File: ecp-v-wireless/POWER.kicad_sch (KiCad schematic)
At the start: 1 part, among them U2 LFE5U-85F-6BG381x

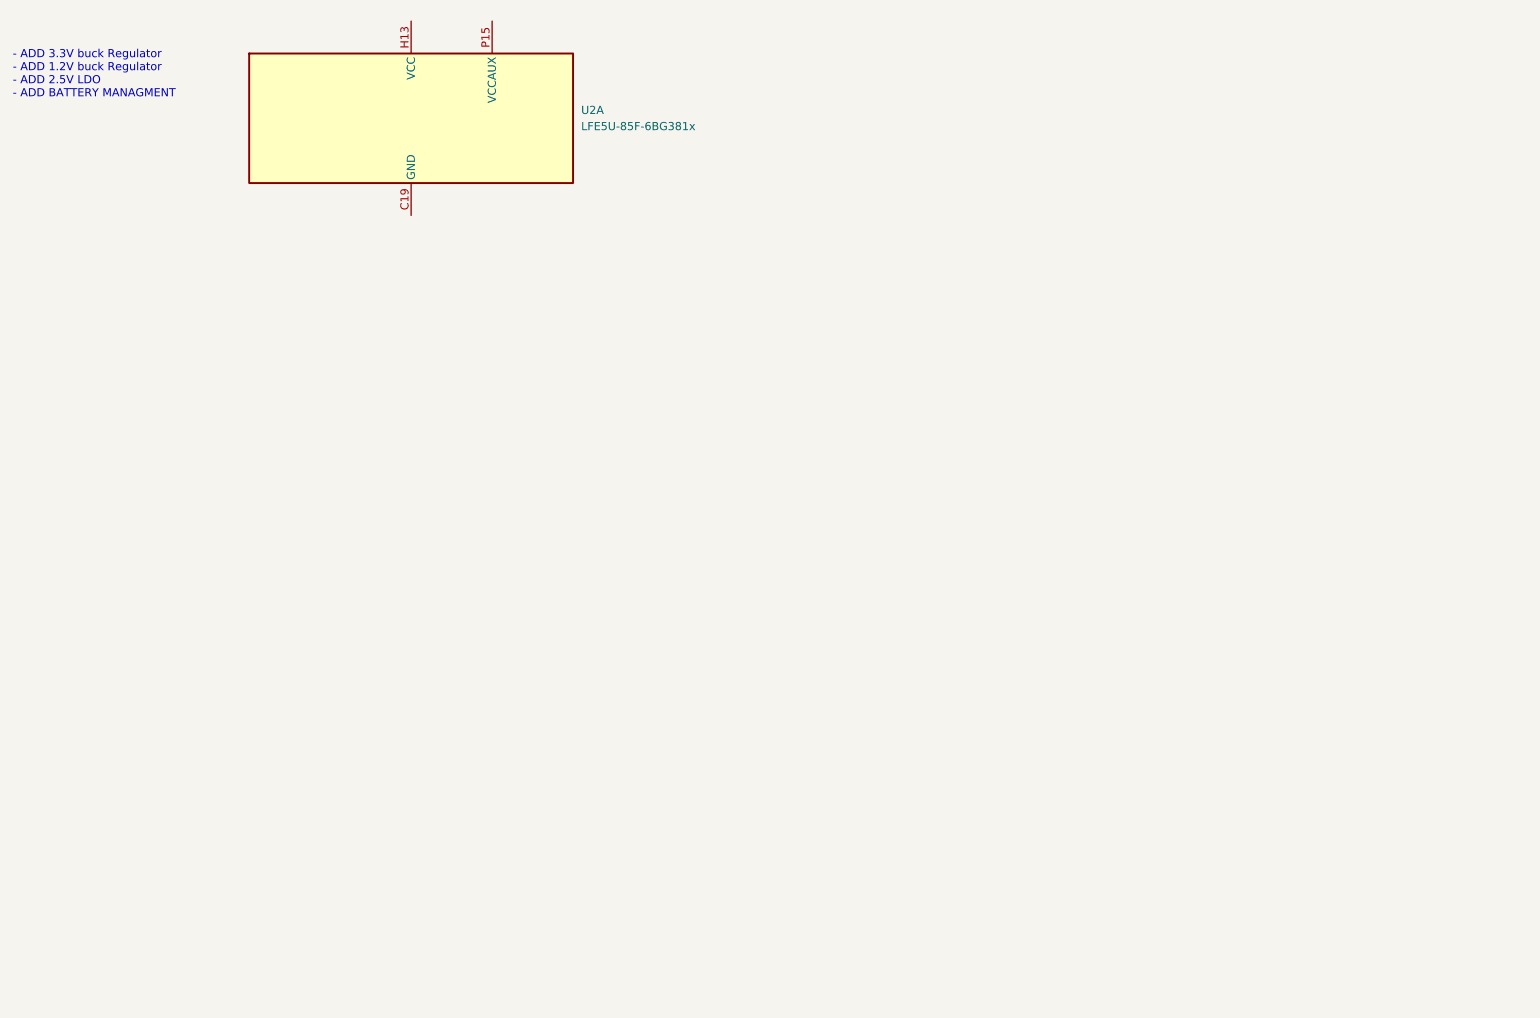
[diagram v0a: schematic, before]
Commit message: Add block diagram, USB, LiPo MGMT, Regs, etc
Signed-off-by: Michael Welling <mwelling79@gmail.com>
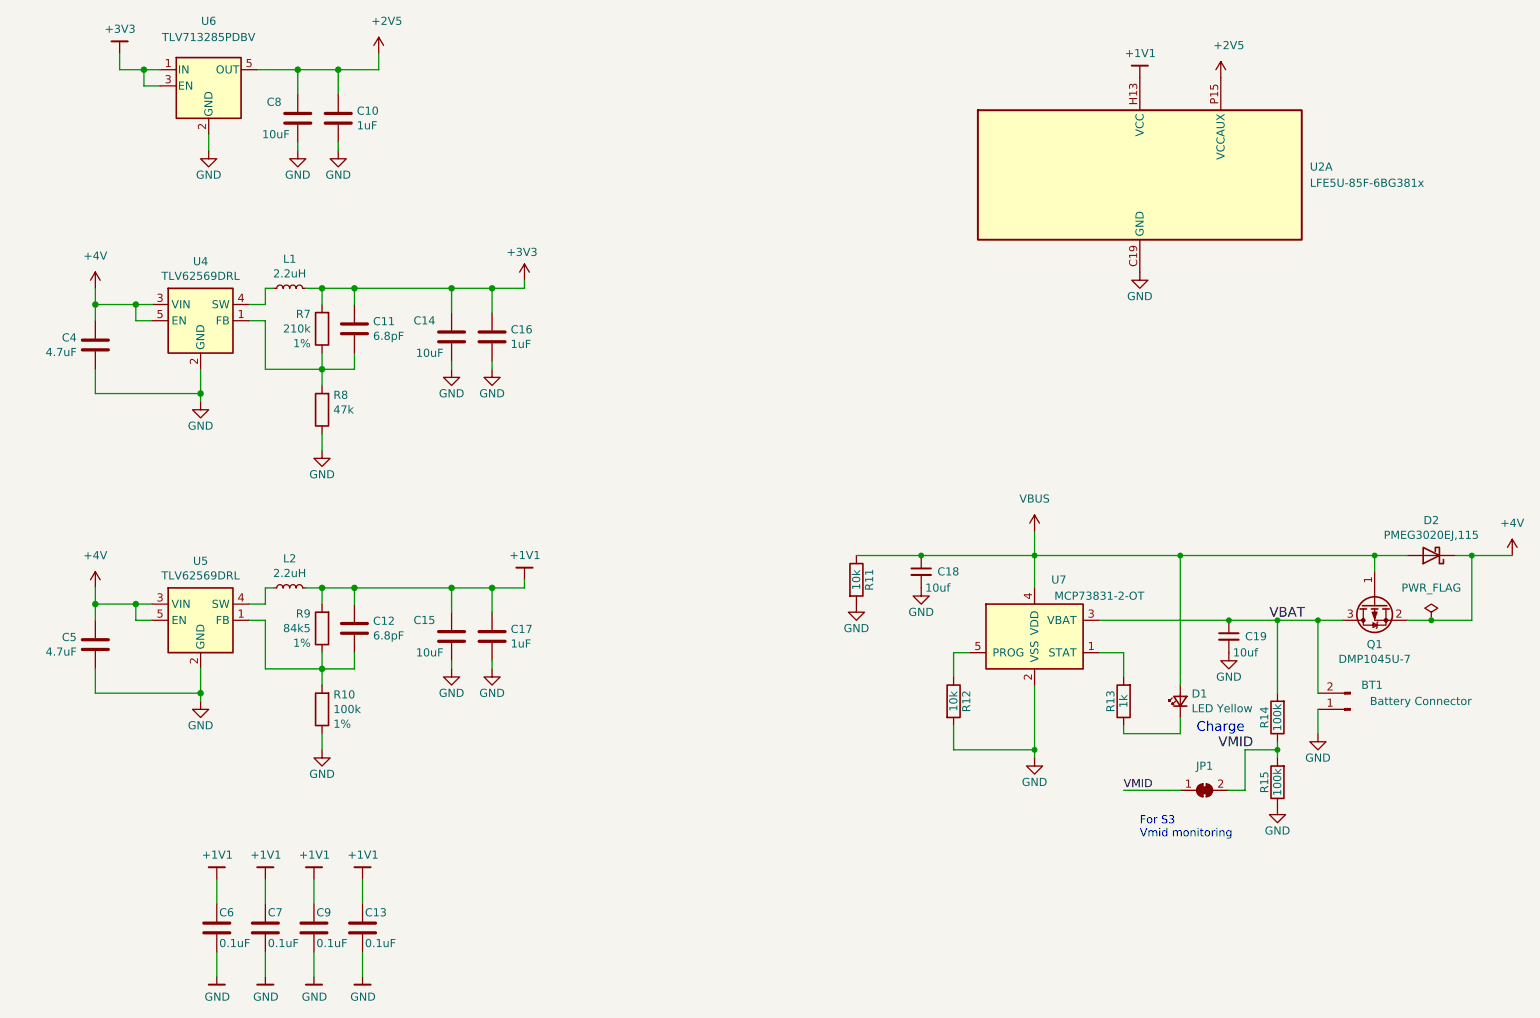
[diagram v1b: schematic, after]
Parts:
- added BT1: Battery Connector, Connector_JST:JST_PH_B2B-PH-SM4-TB_1x02-1MP_P2.00mm_Vertical, symbol Connector:Conn_01x02_Male
- added C10, C16, C17: 1uF, Capacitor_SMD:C_0402_1005Metric, symbol Device:C
- added C11, C12: 6.8pF, Capacitor_SMD:C_0402_1005Metric, symbol Device:C
- added C13, C6, C7, C9: 0.1uF, Capacitor_SMD:C_0402_1005Metric, symbol Device:C
- added C14, C15, C8: 10uF, Capacitor_SMD:C_0603_1608Metric, symbol Device:C
- added C18, C19: 10uf, Capacitor_SMD:C_0805_2012Metric, symbol Device:C_Small
- added C4, C5: 4.7uF, Capacitor_SMD:C_0402_1005Metric, symbol Device:C
- added D1: LED Yellow, LED_SMD:LED_0603_1608Metric, symbol Device:LED_Small
- added D2: PMEG3020EJ,115, Diode_SMD:D_SOD-323F, symbol Device:D_Schottky
- added JP1: SolderJumper_2_Bridged, Jumper:SolderJumper-2_P1.3mm_Bridged_RoundedPad1.0x1.5mm, symbol Jumper:SolderJumper_2_Bridged
- added L1, L2: 2.2uH, Inductor_SMD:L_0805_2012Metric, symbol Device:L_Small
- added Q1: DMP1045U-7, Package_TO_SOT_SMD:SOT-23, symbol Device:Q_PMOS_GSD
- added R10: 100k, Resistor_SMD:R_0402_1005Metric, symbol Device:R
- added R11, R12: 10k, Resistor_SMD:R_0603_1608Metric, symbol Device:R
- added R13: 1k, Resistor_SMD:R_0603_1608Metric, symbol Device:R
- added R14, R15: 100k, Resistor_SMD:R_0603_1608Metric, symbol Device:R
- added R7: 210k, Resistor_SMD:R_0402_1005Metric, symbol Device:R
- added R8: 47k, Resistor_SMD:R_0402_1005Metric, symbol Device:R
- added R9: 84k5, Resistor_SMD:R_0402_1005Metric, symbol Device:R
- added U4, U5: TLV62569DRL, Package_TO_SOT_SMD:SOT-666, symbol Regulator_Switching:TLV62569DRL
- added U6: TLV713285PDBV, Package_TO_SOT_SMD:SOT-23-5, symbol Regulator_Linear:TLV713285PDBV
- added U7: MCP73831-2-OT, Package_TO_SOT_SMD:SOT-23-5, symbol Battery_Management:MCP73831-2-OT
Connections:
- net GND: now reaches U2.B14 (GND), U2.B7 (GND), U2.C19 (GND), U2.D4 (GND), U2.F13 (GND), U2.F14 (GND), U2.F7 (GND), U2.F8 (GND), U2.G10 (GND), U2.G11 (GND), U2.G12 (GND), U2.G13 (GND), U2.G14 (GND), U2.G15 (GND), U2.G17 (GND), U2.G4 (GND), U2.G6 (GND), U2.G7 (GND), U2.G8 (GND), U2.G9 (GND), U2.H19 (GND), U2.J10 (GND), U2.J11 (GND), U2.J12 (GND), U2.J14 (GND), U2.J2 (GND), U2.J7 (GND), U2.J9 (GND), U2.K10 (GND), U2.K11 (GND), U2.K12 (GND), U2.K14 (GND), U2.K15 (GND), U2.K6 (GND), U2.K7 (GND), U2.K9 (GND), U2.L10 (GND), U2.L11 (GND), U2.L12 (GND), U2.L9 (GND), U2.M10 (GND), U2.M11 (GND), U2.M12 (GND), U2.M14 (GND), U2.M16 (GND), U2.M2 (GND), U2.M7 (GND), U2.M9 (GND), U2.N14 (GND), U2.N15 (GND), U2.N6 (GND), U2.N7 (GND), U2.P11 (GND), U2.P12 (GND), U2.P13 (GND), U2.P14 (GND), U2.P7 (GND), U2.P8 (GND), U2.R19 (GND), U2.T10 (GND), U2.T11 (GND), U2.T12 (GND), U2.T13 (GND), U2.T14 (GND), U2.T15 (GND), U2.T6 (GND), U2.T7 (GND), U2.T8 (GND), U2.T9 (GND), U2.U10 (GND), U2.U11 (GND), U2.U12 (GND), U2.U13 (GND), U2.U14 (GND), U2.U15 (GND), U2.U6 (GND), U2.U7 (GND), U2.U8 (GND), U2.U9 (GND), U2.V10 (GND), U2.V11 (GND), U2.V12 (GND), U2.V13 (GND), U2.V14 (GND), U2.V15 (GND), U2.V16 (GND), U2.V17 (GND), U2.V18 (GND), U2.V19 (GND), U2.V20 (GND), U2.V5 (GND), U2.V6 (GND), U2.V7 (GND), U2.V8 (GND), U2.V9 (GND), U2.W12 (GND), U2.W15 (GND), U2.W16 (GND), U2.W19 (GND), U2.W20 (GND), U2.W6 (GND), U2.W7 (GND), U2.Y11 (GND), U2.Y12 (GND), U2.Y14 (GND), U2.Y15 (GND), U2.Y16 (GND), U2.Y17 (GND), U2.Y19 (GND), U2.Y5 (GND), U2.Y6 (GND), U2.Y7 (GND), U2.Y8 (GND)
- net GND: now also BT1.1 (Pin_1), C10.2, C13.2, C14.2, C15.2, C16.2, C17.2, C18.2, C19.2, C4.2, C5.2, C6.2, C7.2, C8.2, C9.2, R10.1, R11.2, R12.2, R15.1, R8.1, U4.2 (GND), U5.2 (GND), U6.2 (GND), U7.2 (VSS)
- net +2V5: now reaches U2.F15 (VCCAUX), U2.F6 (VCCAUX), U2.P15 (VCCAUX), U2.P6 (VCCAUX)
- net +2V5: now also C10.1, C8.1, U6.5 (OUT)
- net +1V1: now reaches U2.H10 (VCC), U2.H11 (VCC), U2.H12 (VCC), U2.H13 (VCC), U2.H8 (VCC), U2.H9 (VCC), U2.J13 (VCC), U2.J8 (VCC), U2.K13 (VCC), U2.K8 (VCC), U2.L13 (VCC), U2.L8 (VCC), U2.M13 (VCC), U2.M8 (VCC), U2.N10 (VCC), U2.N11 (VCC), U2.N12 (VCC), U2.N13 (VCC), U2.N8 (VCC), U2.N9 (VCC)
- net +1V1: now also C12.1, C13.1, C15.1, C17.1, C6.1, C7.1, C9.1, L2.2, R9.2
- new net: R13.2, U7.1 (STAT)
- new net: R12.1, U7.5 (PROG)
- new net: L2.1, U5.4 (SW)
- new net: C11.2, R7.1, R8.2, U4.1 (FB)
- new net: C12.2, R10.2, R9.1, U5.1 (FB)
- new net: D1.1 (K), R13.1
- new net: L1.1, U4.4 (SW)
- new net +3V3: C11.1, C14.1, C16.1, L1.2, R7.2, U6.1 (IN), U6.3 (EN)
- new net +4V: C4.1, C5.1, D2.1 (K), Q1.2 (S), U4.3 (VIN), U4.5 (EN), U5.3 (VIN), U5.5 (EN)
- new net VBAT: BT1.2 (Pin_2), C19.1, Q1.3 (D), R14.2, U7.3 (VBAT)
- new net VBUS: C18.1, D1.2 (A), D2.2 (A), Q1.1 (G), R11.1, U7.4 (VDD)
- new net VMID: JP1.1 (A), JP1.2 (B), R14.1, R15.2
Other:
- note added: "Charge"
- note added: "For S3 Vmid monitoring"
- note removed: "- ADD 3.3V buck Regulator - ADD 1.2V buck Regulator - ADD 2.5V LDO - ADD BATTERY MANAGMENT"
- moved on the sheet: U2A
